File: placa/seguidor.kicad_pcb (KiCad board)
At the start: 2 copper layers, 50 x 50 mm, 3 parts, among them U1 ATmega328P-P, U2 LM7805_TO220, Y1 Crystal

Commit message: circuito modificado
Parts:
- added C1: 100n, Capacitor_THT:C_Disc_D6.0mm_W2.5mm_P5.00mm, F.Cu at (65.0, 61.0)
- added C2: 47u, Capacitor_THT:CP_Radial_D5.0mm_P2.00mm, F.Cu at (79.8, 40.6)
- added C4: 100n, Capacitor_THT:C_Disc_D6.0mm_W2.5mm_P5.00mm, F.Cu at (79.8, 66.0)
- added C5: 22p, Capacitor_THT:C_Disc_D5.0mm_W2.5mm_P5.00mm, F.Cu at (59.4, 67.1)
- added C6: 22p, Capacitor_THT:C_Disc_D5.0mm_W2.5mm_P5.00mm, F.Cu at (59.4, 69.6)
- added D1: LED, LED_THT:LED_D4.0mm, F.Cu at (79.8, 48.8)
- added J2: Conn_01x15_Socket, Connector_PinSocket_2.54mm:PinSocket_1x15_P2.54mm_Horizontal, F.Cu at (96.4, 79.8)
- moved U2 15.0 mm to (69.6, 40.6)
- moved Y1 1.08 mm to (64.0, 66.0)
- moved U1 0.51 mm to (68.6, 45.7)
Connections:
- U1 pad 20: Net-(U1-AVCC) -> +5V
- U1 pad 21: +5V -> Net-(U1-AREF)
- U1 pad 7: Net-(U1-VCC) -> +5V
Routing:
- net +5V: track 0.00 -> 82.3 mm
- net xtal2: track 0.00 -> 10.7 mm
- net xtal1: track 0.00 -> 9.63 mm
- added copper zone on B.Cu, net GND

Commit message: agregados componentes al pcb, faltan conectores
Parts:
- added R1: 3.3k, Resistor_THT:R_Axial_DIN0204_L3.6mm_D1.6mm_P5.08mm_Horizontal, F.Cu at (65.5, 50.8)
- added R2: 3.3k, Resistor_THT:R_Axial_DIN0204_L3.6mm_D1.6mm_P5.08mm_Horizontal, F.Cu at (70.1, 83.3)
- added R3: 3.3k, Resistor_THT:R_Axial_DIN0204_L3.6mm_D1.6mm_P5.08mm_Horizontal, F.Cu at (79.8, 73.7)
- added SW2: btn_arranque, Button_Switch_THT:SW_PUSH_6mm_H5mm, F.Cu at (83.8, 78.7)
- C2: value 47u -> 10u
- moved D1 34.6 mm to (80.8, 83.3), turned to 180 degrees
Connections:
- U1 pad 11: unconnected-(U1-PD5-Pad11) -> motor_izq
- U1 pad 12: unconnected-(U1-PD6-Pad12) -> motor_der
- U1 pad 15: unconnected-(U1-PB1-Pad15) -> arranque
- U1 pad 19: unconnected-(U1-PB5-Pad19) -> led_largada
- U1 pad 21: Net-(U1-AREF) -> unconnected-(U1-AREF-Pad21)
- U1 pad 23: unconnected-(U1-PC0-Pad23) -> sensor4
- U1 pad 24: unconnected-(U1-PC1-Pad24) -> sensor3
- U1 pad 25: unconnected-(U1-PC2-Pad25) -> sensor2
- U1 pad 26: unconnected-(U1-PC3-Pad26) -> sensor1
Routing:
- net +5V: track 82.3 -> 122.5 mm
- net led_largada: track 0.00 -> 17.3 mm
- net arranque: track 0.00 -> 14.1 mm
- net reset: track 0.00 -> 3.12 mm
- net Net-(D1-A): track 0.00 -> 3.05 mm

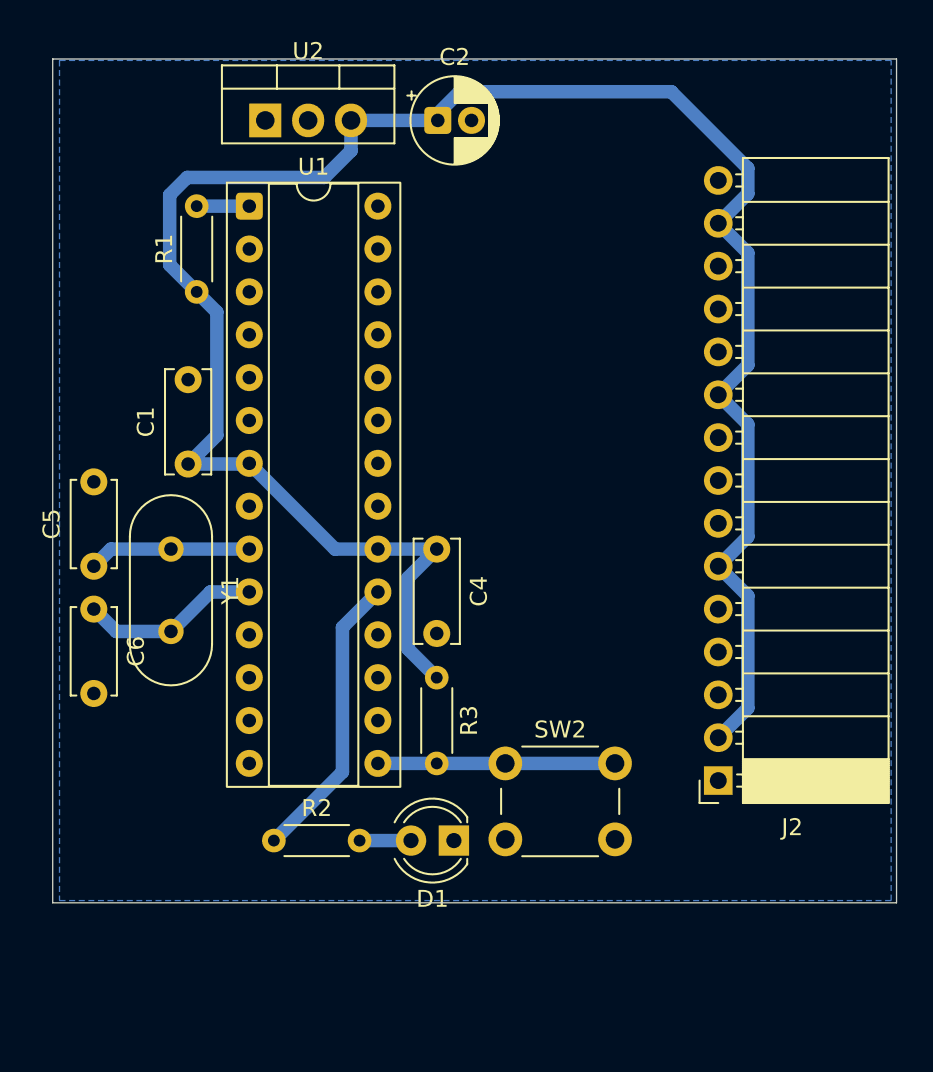
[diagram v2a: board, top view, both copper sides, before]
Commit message: cambiados capacitores en la placa
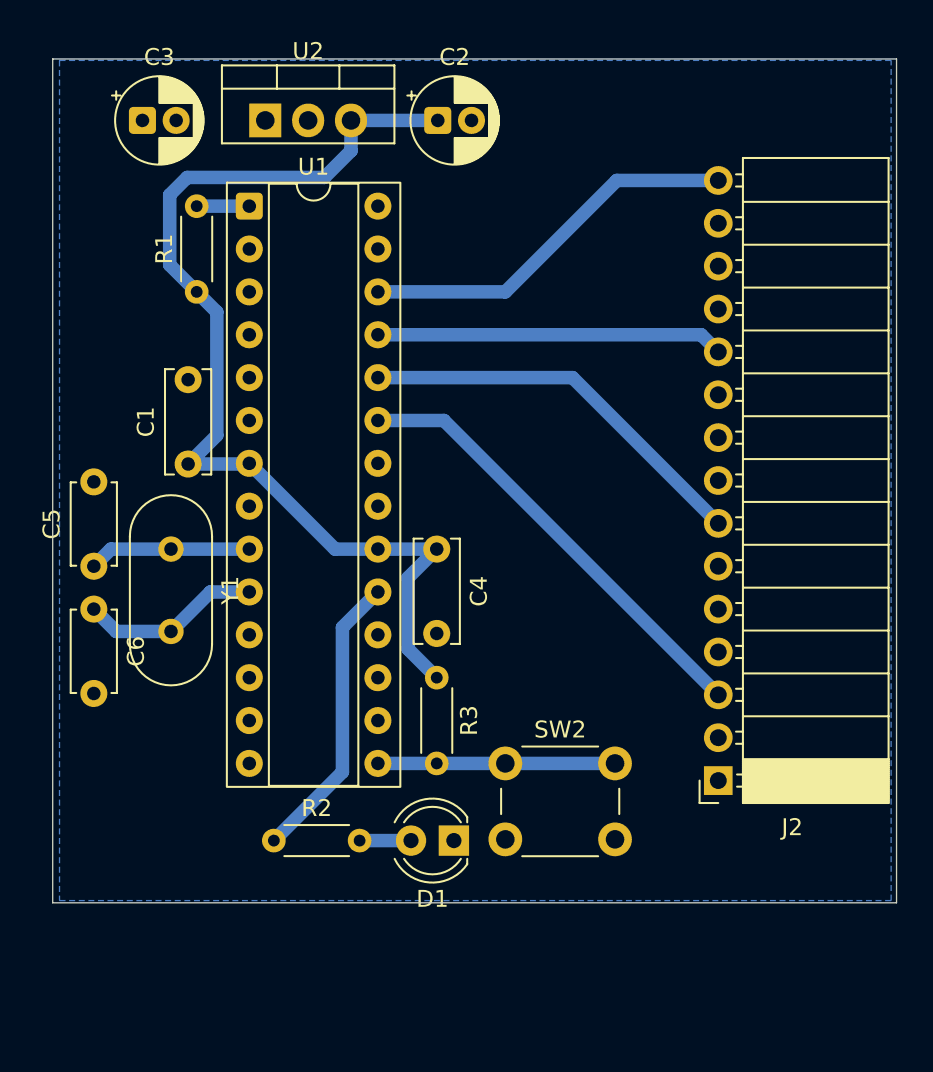
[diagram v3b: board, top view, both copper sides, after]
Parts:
- added C3: 0.33u, Capacitor_THT:CP_Radial_D5.0mm_P2.00mm, F.Cu at (62.3, 40.6)
- C2: value 10u -> 0.1u
- C5, C6: footprint Capacitor_THT:C_Disc_D5.0mm_W2.5mm_P5.00mm -> Capacitor_THT:C_Disc_D4.7mm_W2.5mm_P5.00mm
- J2: value Conn_01x15_Socket -> conn_sensores
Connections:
- U2 pad 1: Net-(J1-Pin_1) -> +BATT
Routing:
- net +5V: track 122.5 -> 62.5 mm
- net sensor4: track 0.00 -> 26.9 mm
- net sensor3: track 0.00 -> 23.7 mm
- net sensor1: track 0.00 -> 22.9 mm
- net sensor2: track 0.00 -> 20.6 mm

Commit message: Tamaño de la placa y agujeros
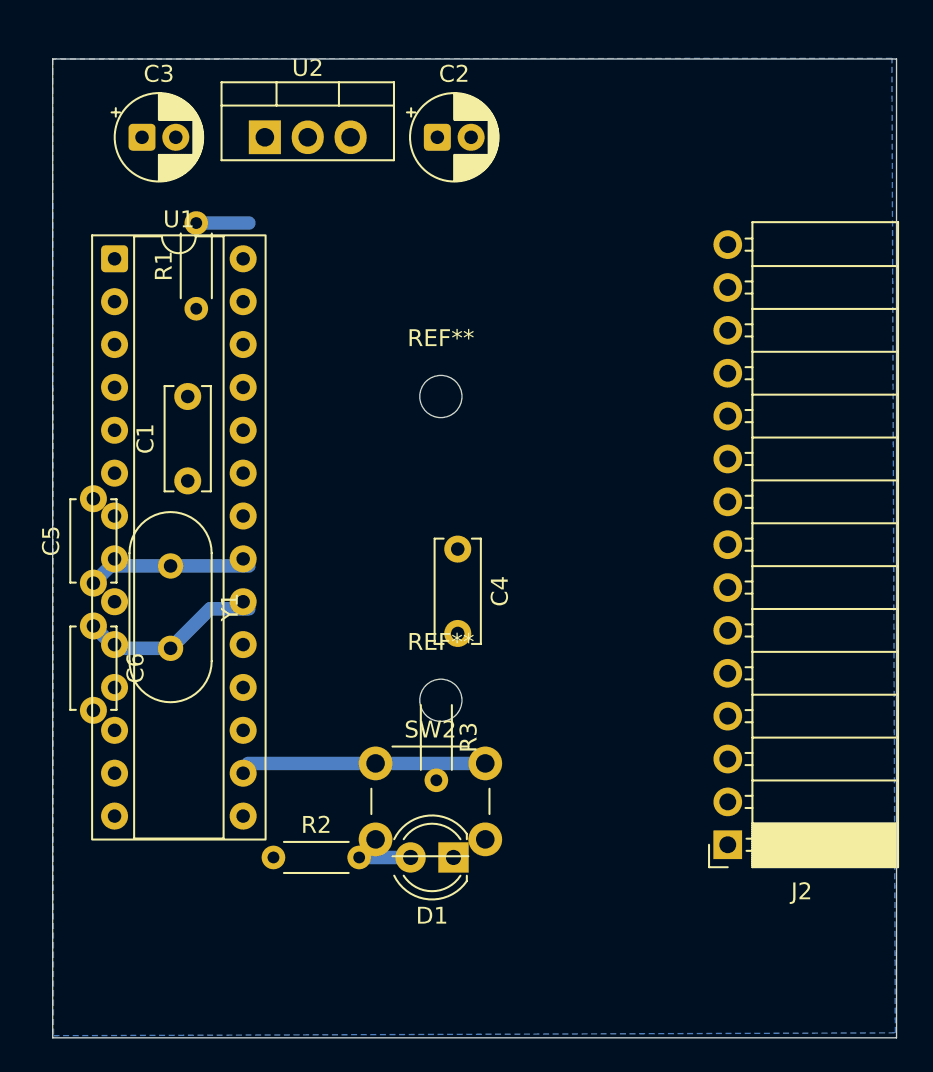
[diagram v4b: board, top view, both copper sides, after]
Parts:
- added REF**: MountingHole_2.5mm, MountingHole:MountingHole_2.5mm, F.Cu at (80.0, 57.0)
- added REF**: MountingHole_2.5mm, MountingHole:MountingHole_2.5mm, F.Cu at (80.0, 75.0)
- moved U1 8.57 mm to (60.7, 48.8)
- moved SW2 7.69 mm to (76.1, 78.7)
- moved J2 3.85 mm to (97.0, 83.6)
- moved C4 1.24 mm to (81.0, 66.0)
- moved C1 1.00 mm to (65.0, 62.0)
- moved C2 1.00 mm to (79.8, 41.6)
- moved C3 1.00 mm to (62.3, 41.6)
- moved C5 1.00 mm to (59.4, 68.1)
- moved C6 1.00 mm to (59.4, 70.6)
- moved D1 1.00 mm to (80.7, 84.3)
- moved R1 1.00 mm to (65.5, 51.8)
- moved R2 1.00 mm to (70.1, 84.3)
- moved R3 1.00 mm to (79.7, 74.7)
- moved U2 1.00 mm to (69.6, 41.6)
- moved Y1 1.00 mm to (64.0, 67.0)
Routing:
- net +5V: track 62.5 -> 0.00 mm
- net sensor4: track 26.9 -> 0.00 mm
- net sensor3: track 23.7 -> 0.00 mm
- net sensor1: track 22.9 -> 0.00 mm
- net sensor2: track 20.6 -> 0.00 mm
- net led_largada: track 17.3 -> 0.00 mm
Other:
- board size 50 x 50 mm -> 50 x 58 mm

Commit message: placa editada
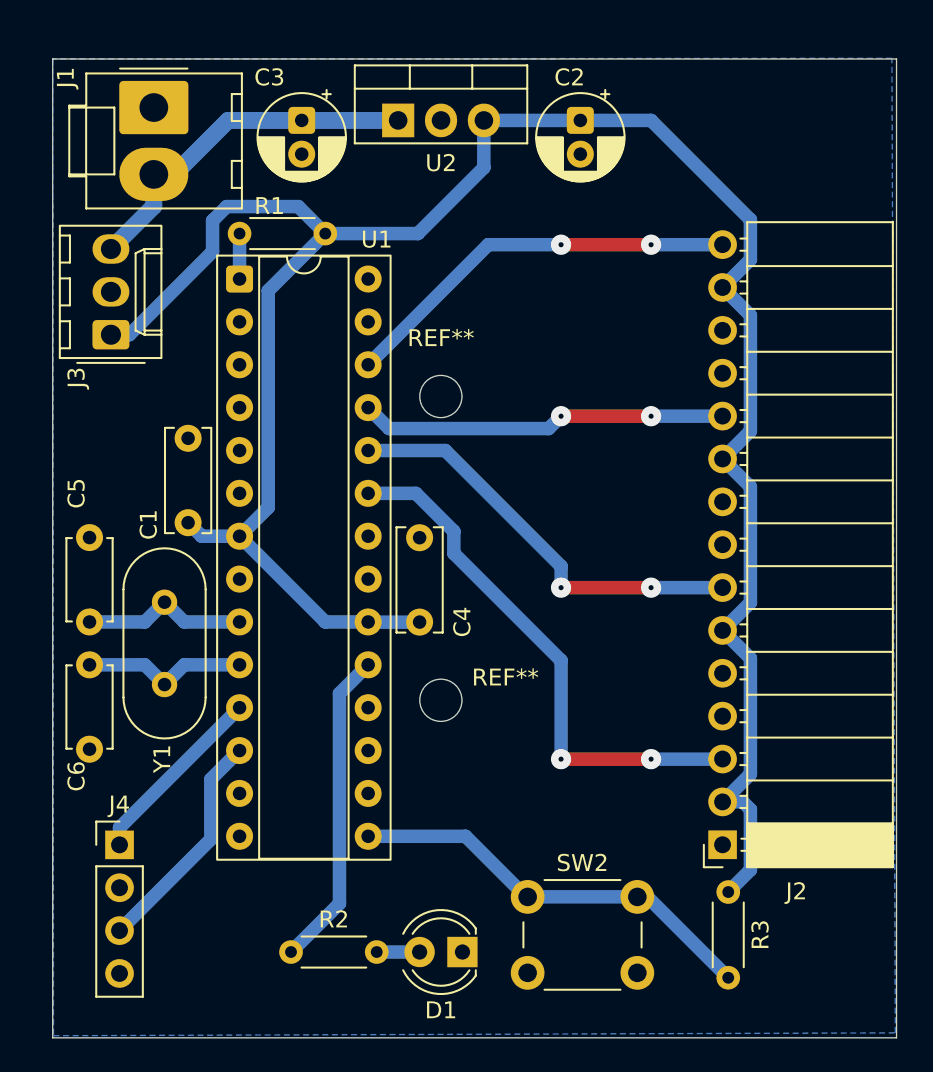
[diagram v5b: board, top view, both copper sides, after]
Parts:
- added J1: conn_bat, Connector_Molex:Molex_KK-396_A-41791-0002_1x02_P3.96mm_Vertical, F.Cu at (63.0, 39.9)
- added J3: conn_motor, Connector_Molex:Molex_KK-254_AE-6410-03A_1x03_P2.54mm_Vertical, F.Cu at (60.5, 53.3)
- added J4: conn_pwm, Connector_PinHeader_2.54mm:PinHeader_1x04_P2.54mm_Vertical, F.Cu at (61.0, 83.6)
- moved R3 20.9 mm to (97.0, 86.4)
- moved SW2 12.0 mm to (85.1, 86.7)
- moved C3 9.51 mm to (71.8, 40.6), turned to -90 degrees
- moved R1 8.85 mm to (73.2, 47.3), turned to 180 degrees
- moved C2 8.53 mm to (88.3, 40.6), turned to -90 degrees
- moved U2 7.96 mm to (77.5, 40.6)
- moved U1 7.50 mm to (68.1, 50.0)
- moved R2 5.70 mm to (71.1, 89.9)
- moved D1 5.63 mm to (81.3, 89.9)
- moved C4 4.88 mm to (78.7, 70.4), turned to 90 degrees
- moved C1 2.48 mm to (65.0, 64.5)
- moved C5 2.31 mm to (59.2, 70.4)
- moved C6 2.31 mm to (59.2, 72.9)
- moved Y1 2.18 mm to (63.6, 69.2)
- moved J2 0.31 mm to (96.7, 83.6)
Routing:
- net +5V: track 0.00 -> 132.4 mm
- net sensor4: track 0.00 -> 31.7 mm, vias 0 -> 2
- net sensor3: track 0.00 -> 25.1 mm, vias 0 -> 2
- net sensor1: track 0.00 -> 24.0 mm, vias 0 -> 2
- net sensor2: track 0.00 -> 21.8 mm, vias 0 -> 2
- net +BATT: track 0.00 -> 21.3 mm
- net led_largada: track 0.00 -> 18.9 mm
- net motor_der: track 0.00 -> 13.6 mm
- net motor_izq: track 0.00 -> 11.1 mm
- net arranque: track 14.1 -> 24.8 mm
- net xtal2: track 10.7 -> 9.86 mm
- net Net-(D1-A): track 3.05 -> 2.54 mm
